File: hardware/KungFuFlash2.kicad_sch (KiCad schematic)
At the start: 52 parts, among them J1 SWD, J2 USB_B_Micro, J3 Wifi, Q1 BC817, SW1 Reset, SW2 Menu, SW3 Special, U1 C64-Exp-Port, U2 AMS1117-3.3, U3 STM32H7B0VBTx, Y1 25MHz

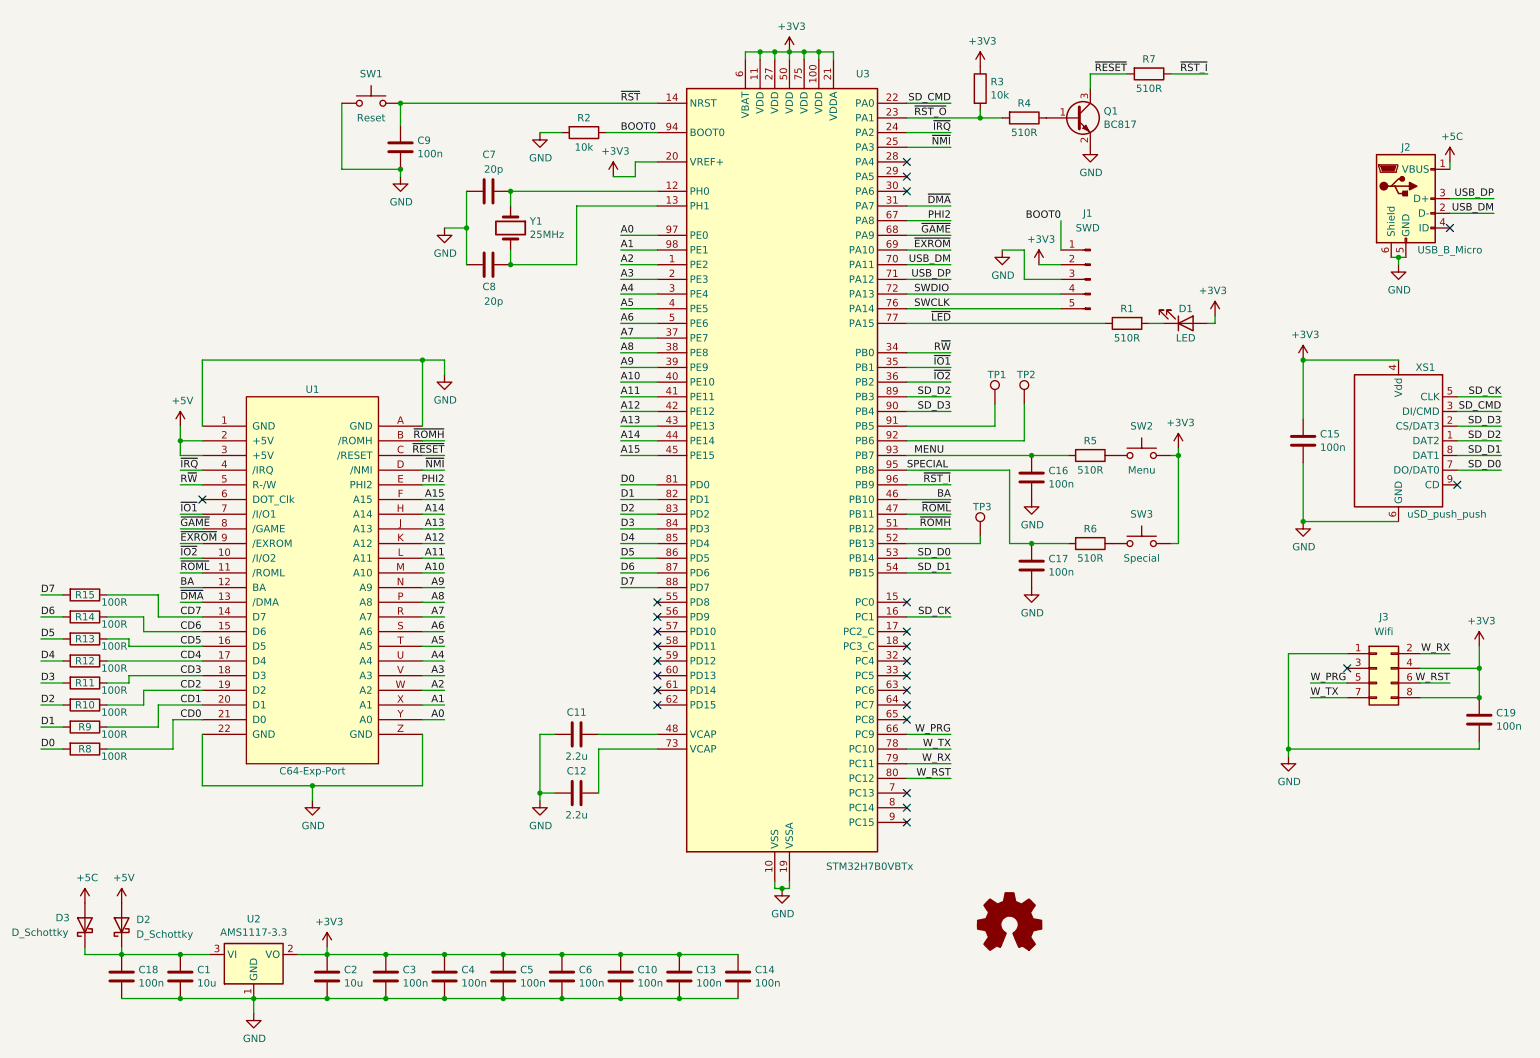
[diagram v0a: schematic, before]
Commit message: added USB-C connector
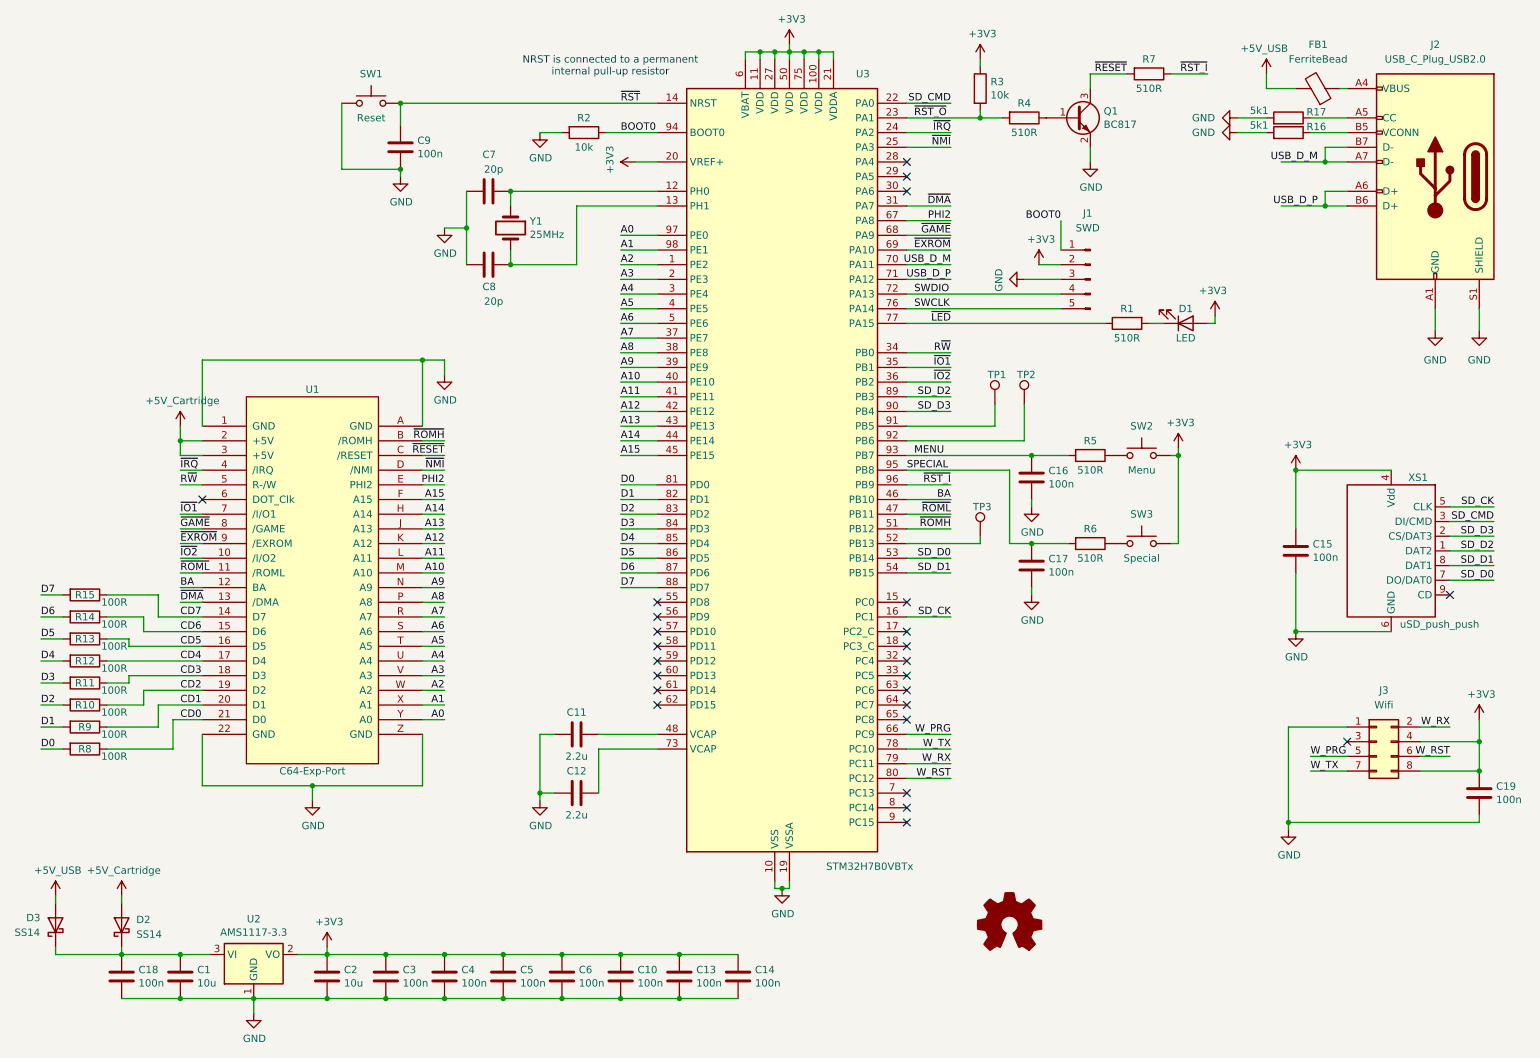
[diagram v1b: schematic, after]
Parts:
- removed J2: USB_B_Micro, KungFuFlash2:Conn_USBmicro-B_ebay-side_TH, symbol KungFuFlash2:USB_B_Micro-Connector
- added FB1: FerriteBead, Inductor_SMD:L_0805_2012Metric_Pad1.15x1.40mm_HandSolder, symbol Device:FerriteBead
- added J2: USB_C_Plug_USB2.0, Connector_USB:USB_C_Receptacle_GCT_USB4105-xx-A_16P_TopMnt_Horizontal, symbol Connector:USB_C_Plug_USB2.0
- added R16, R17: 5k1, Resistor_SMD:R_0805_2012Metric_Pad1.20x1.40mm_HandSolder, symbol Device:R
- C1, C2: LCSC (none) -> C19702
- C10, C13, C14, C15, C16, C17, C18, C19, C3, C4, C5, C6, C9: LCSC (none) -> C38898
- C11, C12: LCSC (none) -> C19110
- C7, C8: LCSC (none) -> C105621
- D1: LCSC (none) -> C84256
- D2, D3: value D_Schottky -> SS14; LCSC (none) -> C2480
- J1: LCSC (none) -> C492404
- J3: LCSC (none) -> C18723055; now left out of the parts list
- Q1: LCSC (none) -> C52801
- R1, R4, R5, R6, R7: LCSC (none) -> C17734
- R10, R11, R12, R13, R14, R15, R8, R9: LCSC (none) -> C17408
- R2, R3: LCSC (none) -> C17414
- SW1, SW2, SW3: LCSC (none) -> C285486
- U1: now left out of the parts list
- U2: LCSC (none) -> C347222
- U3: LCSC (none) -> C730227
- Y1: LCSC (none) -> C251592
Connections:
- net GND: now also J2.A1 (GND), J2.A12 (GND), J2.B1 (GND), J2.B12 (GND), J2.S1 (SHIELD), R16.2, R17.2
- net +5C renamed +5V_USB
- net +5V_USB: now also FB1.2
- net +5V renamed +5V_Cartridge
- net USB_DM renamed USB_D_M
- net USB_D_M: now also J2.A7 (D-), J2.B7 (D-)
- net USB_DP renamed USB_D_P
- net USB_D_P: now also J2.A6 (D+), J2.B6 (D+)
- new net: J2.A5 (CC), R17.1
- new net: FB1.1, J2.A4 (VBUS), J2.A9 (VBUS), J2.B4 (VBUS), J2.B9 (VBUS)
- new net: J2.B5 (VCONN), R16.1
- no-connect marks 26 -> 25
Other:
- note added: "NRST is connected to a permanent internal pull-up resistor"
- moved on the sheet: C15, C19, D3, J3, XS1
